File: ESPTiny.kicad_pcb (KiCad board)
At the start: 2 copper layers, 2 parts, among them J1 Conn_01x10_Male, U1 ESP-01v090

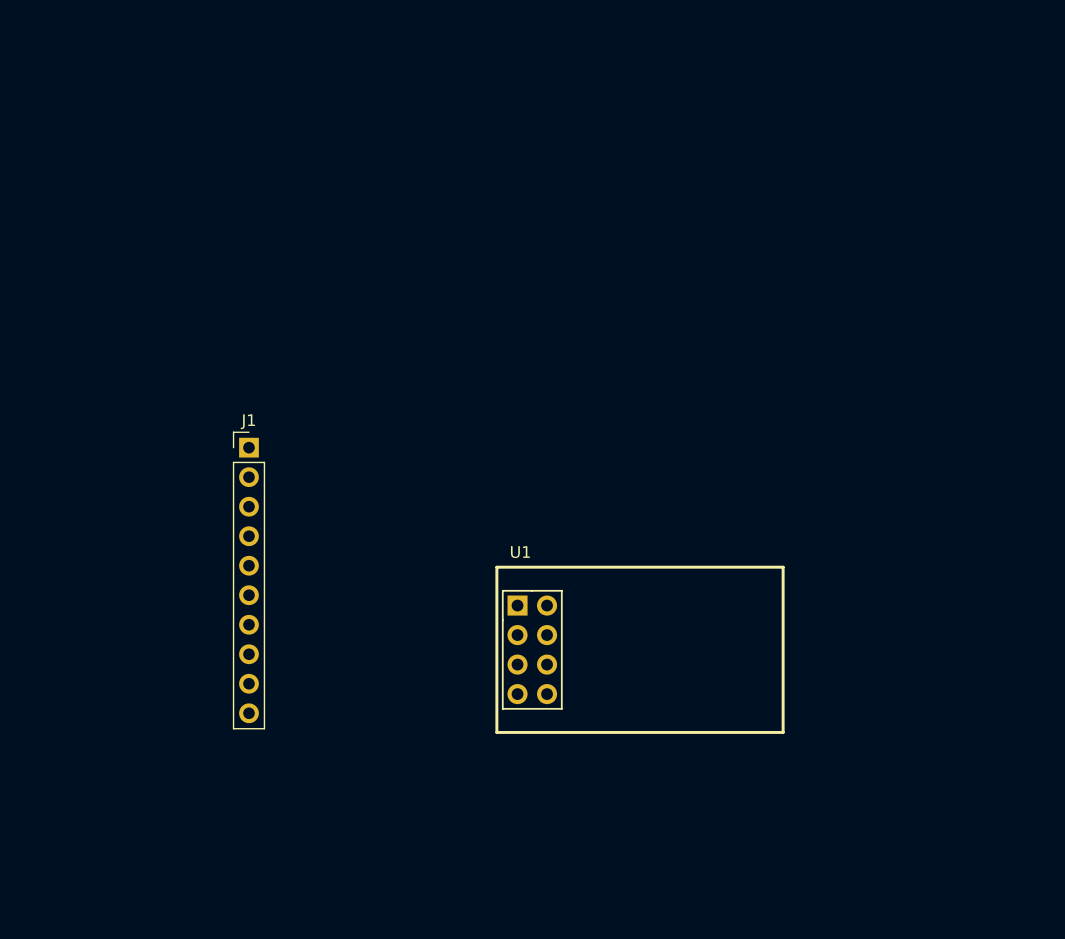
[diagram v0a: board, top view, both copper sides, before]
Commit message: Add footprints
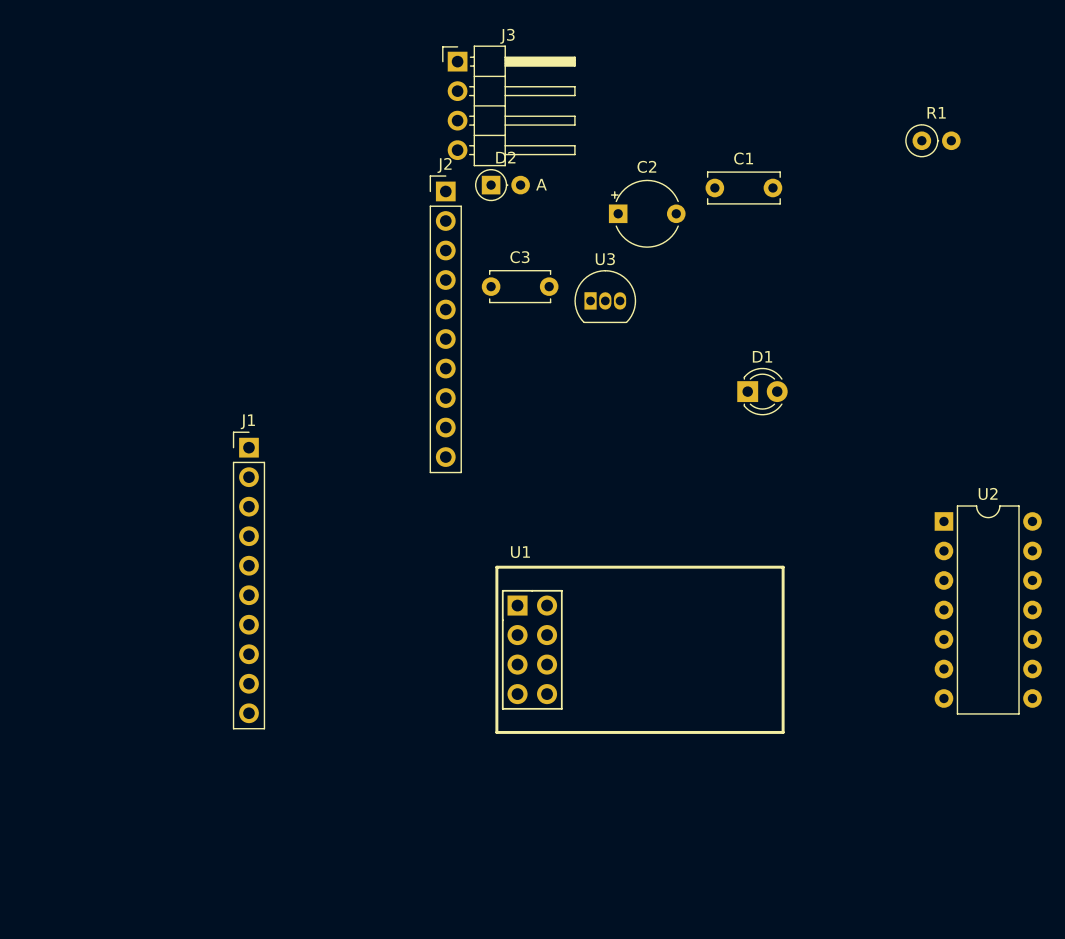
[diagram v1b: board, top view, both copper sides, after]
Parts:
- added C1: 1u, Capacitor_THT:C_Disc_D6.0mm_W2.5mm_P5.00mm, F.Cu at (92.8, 4.19)
- added C2: 100u, Capacitor_THT:CP_Radial_Tantal_D5.5mm_P5.00mm, F.Cu at (84.5, 6.41)
- added C3: 100n, Capacitor_THT:C_Disc_D5.0mm_W2.5mm_P5.00mm, F.Cu at (73.5, 12.7)
- added D1: LED, LED_THT:LED_D3.0mm, F.Cu at (95.6, 21.7)
- added D2: BAT85, Diode_THT:D_DO-35_SOD27_P2.54mm_Vertical_AnodeUp, F.Cu at (73.5, 3.94)
- added J2: Conn_01x10_Male, Connector_PinHeader_2.54mm:PinHeader_1x10_P2.54mm_Vertical, F.Cu at (69.6, 4.49)
- added J3: Conn_01x04_Male, Connector_PinHeader_2.54mm:PinHeader_1x04_P2.54mm_Horizontal, F.Cu at (70.7, -6.68)
- added R1: 220, Resistor_THT:R_Axial_DIN0207_L6.3mm_D2.5mm_P2.54mm_Vertical, F.Cu at (110.6, 0.13)
- added U2: ATtiny84-20PU, Package_DIP:DIP-14_W7.62mm, F.Cu at (112.5, 32.9)
- added U3: MCP1700-3302E_TO92, Package_TO_SOT_THT:TO-92_Inline, F.Cu at (82.1, 13.9)

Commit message: Without power divider
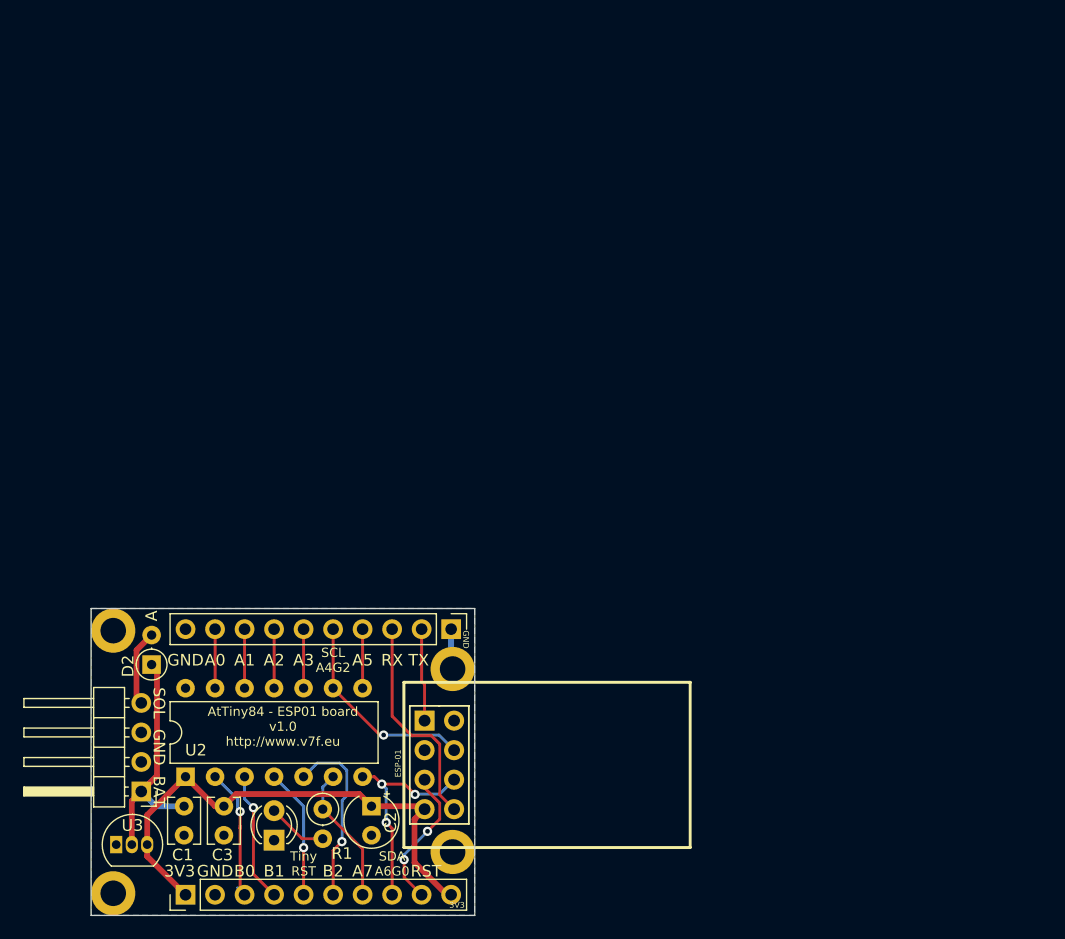
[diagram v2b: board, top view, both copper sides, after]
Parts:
- added REF**: MountingHole_2.2mm_M2_DIN965_Pad, MountingHole:MountingHole_2.2mm_M2_DIN965_Pad, F.Cu at (41.0, 42.3)
- added REF**: MountingHole_2.2mm_M2_DIN965_Pad, MountingHole:MountingHole_2.2mm_M2_DIN965_Pad, F.Cu at (41.0, 64.9)
- added REF**: MountingHole_2.2mm_M2_DIN965_Pad, MountingHole:MountingHole_2.2mm_M2_DIN965_Pad, F.Cu at (70.2, 61.3)
- added REF**: MountingHole_2.2mm_M2_DIN965_Pad, MountingHole:MountingHole_2.2mm_M2_DIN965_Pad, F.Cu at (70.2, 45.6)
- C1: footprint Capacitor_THT:C_Disc_D6.0mm_W2.5mm_P5.00mm -> Capacitor_THT:C_Disc_D3.8mm_W2.6mm_P2.50mm
- C2: footprint Capacitor_THT:CP_Radial_Tantal_D5.5mm_P5.00mm -> Capacitor_THT:CP_Radial_Tantal_D4.5mm_P2.50mm
- C3: footprint Capacitor_THT:C_Disc_D5.0mm_W2.5mm_P5.00mm -> Capacitor_THT:C_Disc_D3.8mm_W2.6mm_P2.50mm
- moved R1 77.3 mm to (59.1, 57.7), turned to 270 degrees
- moved C1 70.1 mm to (47.1, 57.4), turned to 270 degrees
- moved U2 68.9 mm to (47.2, 54.9), turned to 90 degrees
- moved J3 68.5 mm to (43.4, 56.1), turned to 180 degrees
- moved U3 62.0 mm to (41.4, 60.7)
- moved D1 56.1 mm to (54.9, 60.3), turned to 90 degrees
- moved C2 55.2 mm to (63.2, 57.4), turned to 270 degrees
- moved D2 50.6 mm to (44.3, 45.2), turned to 90 degrees
- moved C3 50.3 mm to (50.5, 57.4), turned to 270 degrees
- moved J1 38.9 mm to (47.2, 65.0), turned to 90 degrees
- moved J2 37.7 mm to (70.1, 42.2), turned to 270 degrees
- moved U1 12.7 mm to (67.8, 50.0)
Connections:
- C1 pad 1: Net-(C1-Pad1) -> +BATT
- C1 pad 2: Net-(C1-Pad2) -> GND
- C2 pad 1: Net-(C2-Pad1) -> +3V3
- C2 pad 2: Net-(C2-Pad2) -> GND
- C3 pad 1: Net-(C3-Pad1) -> +3V3
- C3 pad 2: Net-(C3-Pad2) -> GND
- D1 pad 1: Net-(D1-Pad1) -> GND
- D2 pad 1: Net-(D2-Pad1) -> +BATT
- J1 pad 1: Net-(J1-Pad1) -> +3V3
- J1 pad 10: Net-(J1-Pad10) -> +3V3
- J1 pad 2: Net-(J1-Pad2) -> GND
- J1 pad 3: Net-(J1-Pad3) -> /B0
- J1 pad 4: Net-(J1-Pad4) -> /B1
- J1 pad 5: Net-(J1-Pad5) -> /TRST
- J1 pad 6: Net-(J1-Pad6) -> /B2
- J1 pad 7: Net-(J1-Pad7) -> /A7
- J1 pad 8: Net-(J1-Pad8) -> /SDA-A6
- J1 pad 9: Net-(J1-Pad9) -> /RST
- J2 pad 1: Net-(J2-Pad1) -> GND
- J2 pad 10: Net-(J2-Pad10) -> GND
- J2 pad 2: Net-(J2-Pad2) -> /TX
- J2 pad 3: Net-(J2-Pad3) -> /RX
- J2 pad 4: Net-(J2-Pad4) -> /A5
- J2 pad 5: Net-(J2-Pad5) -> /SCL-A4
- J2 pad 6: Net-(J2-Pad6) -> /A3
- J2 pad 7: Net-(J2-Pad7) -> /A2
- J2 pad 8: Net-(J2-Pad8) -> /A1
- J2 pad 9: Net-(J2-Pad9) -> /A0
- J3 pad 1: Net-(J3-Pad1) -> +BATT
- J3 pad 2: Net-(J3-Pad2) -> GND
- J3 pad 3: Net-(J3-Pad3) -> GND
- J3 pad 4: Net-(J3-Pad4) -> Net-(D2-Pad2)
- R1 pad 1: Net-(R1-Pad1) -> /A7
- R1 pad 2: Net-(R1-Pad2) -> Net-(D1-Pad2)
- U1 pad 1: Net-(U1-Pad1) -> /TX
- U1 pad 3: Net-(U1-Pad3) -> GND
- U1 pad 4: Net-(U1-Pad4) -> /SCL-A4
- U1 pad 5: Net-(U1-Pad5) -> /RST
- U1 pad 6: Net-(U1-Pad6) -> /SDA-A6
- U1 pad 8: Net-(U1-Pad8) -> /RX
- U2 pad 1: Net-(U2-Pad1) -> +3V3
- U2 pad 10: Net-(U2-Pad10) -> /A3
- U2 pad 11: Net-(U2-Pad11) -> /A2
- U2 pad 12: Net-(U2-Pad12) -> /A1
- U2 pad 13: Net-(U2-Pad13) -> /A0
- U2 pad 14: Net-(U2-Pad14) -> GND
- U2 pad 2: Net-(U2-Pad2) -> /B0
- U2 pad 3: Net-(U2-Pad3) -> /B1
- U2 pad 4: Net-(U2-Pad4) -> /TRST
- U2 pad 5: Net-(U2-Pad5) -> /B2
- U2 pad 6: Net-(U2-Pad6) -> /A7
- U2 pad 7: Net-(U2-Pad7) -> /SDA-A6
- U2 pad 8: Net-(U2-Pad8) -> /A5
- U2 pad 9: Net-(U2-Pad9) -> /SCL-A4
- U3 pad 1: Net-(U3-Pad1) -> GND
- U3 pad 2: Net-(U3-Pad2) -> +BATT
- U3 pad 3: Net-(U3-Pad3) -> +3V3
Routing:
- net +3V3: track 0.00 -> 45.1 mm
- net +BATT: track 0.00 -> 21.2 mm
- net /SDA-A6: track 0.00 -> 18.9 mm, vias 0 -> 3
- net /RX: track 0.00 -> 18.7 mm
- net /SCL-A4: track 0.00 -> 18.0 mm, vias 0 -> 1
- net /B2: track 0.00 -> 15.7 mm, vias 0 -> 1
- net /RST: track 0.00 -> 12.4 mm, vias 0 -> 2
- net /B0: track 0.00 -> 12.3 mm, vias 0 -> 1
- net /A7: track 0.00 -> 11.9 mm
- net /TRST: track 0.00 -> 11.9 mm, vias 0 -> 1
- net /B1: track 0.00 -> 11.8 mm, vias 0 -> 1
- net /TX: track 0.00 -> 7.98 mm
- net Net-(D2-Pad2): track 0.00 -> 6.69 mm
- net Net-(D1-Pad2): track 0.00 -> 5.19 mm
- net /A5: track 0.00 -> 5.08 mm
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- added copper zone on B.Cu, net GND
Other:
- board outline added: 33 x 26.4 mm
- net class Default: clearance 0.2 -> 0.25
- net class power added: clearance 0.25, trace_width 0.5, via_dia 0.8, via_drill 0.4
- rule trace_clearance: 0.2 -> 0.25
- rule trace_min: 0.2 -> 0.25
- board text added: "3V3"
- board text added: "A0"
- board text added: "A1"
- board text added: "A2"
- board text added: "A3"
- board text added: "A5"
- board text added: "A7"
- board text added: "AtTiny84 - ESP01 board v1.0 http://www.v7f.eu"
- board text added: "B0"
- board text added: "B1"
- board text added: "B2"
- board text added: "BAT"
- board text added: "ESP-01"
- board text added: "GND"
- board text added: "RST"
- board text added: "RX"
- board text added: "SCL A4G2"
- board text added: "SDA A6G0"
- board text added: "SOL"
- board text added: "TX"
- board text added: "Tiny RST"

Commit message: With power divider
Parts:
- added R2: 220, Resistor_THT:R_Axial_DIN0207_L6.3mm_D2.5mm_P2.54mm_Vertical, F.Cu at (49.9, 44.8)
- added R3: 220, Resistor_THT:R_Axial_DIN0207_L6.3mm_D2.5mm_P2.54mm_Vertical, F.Cu at (55.1, 44.8)
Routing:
- net +BATT: track 21.2 -> 24.4 mm
- net /A1: track 5.08 -> 7.96 mm
- net /A2: track 5.08 -> 6.26 mm
- net /A0: track 5.08 -> 5.95 mm
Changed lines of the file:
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@@
     (thickness 1.6)
     (drawings 49)
-    (tracks 122)
+    (tracks 133)
     (zones 0)
-    (modules 16)
+    (modules 18)
     (nets 21)
   )
@@
   )
   (layers
-    (0 F.Cu signal hide)
-    (31 B.Cu signal hide)
+    (0 F.Cu signal)
+    (31 B.Cu signal)
     (32 B.Adhes user)
     (33 F.Adhes user)
@@
       (effects (font (size 1 1) (thickness 0.15)))
     )
-    (fp_text user A (at 4.191 0 90) (layer F.SilkS)
+    (fp_text user A (at 4.064 0 90) (layer F.SilkS)
       (effects (font (size 1 1) (thickness 0.15)))
     )
@@
     )
   )
+  (module Resistor_THT:R_Axial_DIN0207_L6.3mm_D2.5mm_P2.54mm_Vertical (layer F.Cu)
+    (at 49.911 44.831 180)
+    (descr "Resistor, Axial_DIN0207 series, Axial, Vertical, pin pitch=2.54mm, 0.25W = 1/4W, length*diameter=6.3*2.5mm^2, http://cdn-reichelt.de/documents/datenblatt/B400/1_4W%23YAG.pdf")
+    (tags "Resistor Axial_DIN0207 series Axial Vertical pin pitch 2.54mm 0.25W = 1/4W length 6.3mm diameter 2.5mm")
+    (fp_text reference R2 (at 1.397 -1.27) (layer F.SilkS)
+      (effects (font (size 0.5 0.5) (thickness 0.125)))
+    )
+    (fp_text value 220 (at 1.27 2.37) (layer F.Fab)
+      (effects (font (size 1 1) (thickness 0.15)))
+    )
+    (fp_line (start 3.59 -1.5) (end -1.5 -1.5) (layer F.CrtYd) (width 0.05))
+    (fp_line (start 3.59 1.5) (end 3.59 -1.5) (layer F.CrtYd) (width 0.05))
+    (fp_line (start -1.5 1.5) (end 3.59 1.5) (layer F.CrtYd) (width 0.05))
+    (fp_line (start -1.5 -1.5) (end -1.5 1.5) (layer F.CrtYd) (width 0.05))
+    (fp_line (start 1.37 0) (end 1.44 0) (layer F.SilkS) (width 0.12))
+    (fp_line (start 0 0) (end 2.54 0) (layer F.Fab) (width 0.1))
+    (fp_circle (center 0 0) (end 1.37 0) (layer F.SilkS) (width 0.12))
+    (fp_circle (center 0 0) (end 1.25 0) (layer F.Fab) (width 0.1))
+    (fp_text user %R (at 1.27 -2.37) (layer F.Fab)
+      (effects (font (size 1 1) (thickness 0.15)))
+    )
+    (pad 1 thru_hole circle (at 0 0 180) (size 1.6 1.6) (drill 0.8) (layers *.Cu *.Mask)
+      (net 19 /A1))
+    (pad 2 thru_hole oval (at 2.54 0 180) (size 1.6 1.6) (drill 0.8) (layers *.Cu *.Mask)
+      (net 5 +BATT))
+    (model ${KISYS3DMOD}/Resistor_THT.3dshapes/R_Axial_DIN0207_L6.3mm_D2.5mm_P2.54mm_Vertical.wrl
+      (at (xyz 0 0 0))
+      (scale (xyz 1 1 1))
+      (rotate (xyz 0 0 0))
+    )
+  )
+  (module Resistor_THT:R_Axial_DIN0207_L6.3mm_D2.5mm_P2.54mm_Vertical (layer F.Cu)
+    (at 55.118 44.831 180)
+    (descr "Resistor, Axial_DIN0207 series, Axial, Vertical, pin pitch=2.54mm, 0.25W = 1/4W, length*diameter=6.3*2.5mm^2, http://cdn-reichelt.de/documents/datenblatt/B400/1_4W%23YAG.pdf")
+    (tags "Resistor Axial_DIN0207 series Axial Vertical pin pitch 2.54mm 0.25W = 1/4W length 6.3mm diameter 2.5mm")
+    (fp_text reference R3 (at 1.651 -1.27) (layer F.SilkS)
+      (effects (font (size 0.5 0.5) (thickness 0.125)))
+    )
+    (fp_text value 220 (at 1.27 2.37) (layer F.Fab)
+      (effects (font (size 1 1) (thickness 0.15)))
+    )
+    (fp_text user %R (at 1.27 -2.37) (layer F.Fab)
+      (effects (font (size 1 1) (thickness 0.15)))
+    )
+    (fp_circle (center 0 0) (end 1.25 0) (layer F.Fab) (width 0.1))
+    (fp_circle (center 0 0) (end 1.37 0) (layer F.SilkS) (width 0.12))
+    (fp_line (start 0 0) (end 2.54 0) (layer F.Fab) (width 0.1))
+    (fp_line (start 1.37 0) (end 1.44 0) (layer F.SilkS) (width 0.12))
+    (fp_line (start -1.5 -1.5) (end -1.5 1.5) (layer F.CrtYd) (width 0.05))
+    (fp_line (start -1.5 1.5) (end 3.59 1.5) (layer F.CrtYd) (width 0.05))
+    (fp_line (start 3.59 1.5) (end 3.59 -1.5) (layer F.CrtYd) (width 0.05))
+    (fp_line (start 3.59 -1.5) (end -1.5 -1.5) (layer F.CrtYd) (width 0.05))
+    (pad 2 thru_hole oval (at 2.54 0 180) (size 1.6 1.6) (drill 0.8) (layers *.Cu *.Mask)
+      (net 19 /A1))
+    (pad 1 thru_hole circle (at 0 0 180) (size 1.6 1.6) (drill 0.8) (layers *.Cu *.Mask)
+      (net 1 GND))
+    (model ${KISYS3DMOD}/Resistor_THT.3dshapes/R_Axial_DIN0207_L6.3mm_D2.5mm_P2.54mm_Vertical.wrl
+      (at (xyz 0 0 0))
+      (scale (xyz 1 1 1))
+      (rotate (xyz 0 0 0))
+    )
+  )
   (gr_text GND (at 71.374 43.053 270) (layer B.SilkS)
     (effects (font (size 0.5 0.5) (thickness 0.125)) (justify mirror))
@@
     (effects (font (size 1 1) (thickness 0.15)) (justify mirror))
   )
-  (gr_text A2 (at 54.864 44.831) (layer B.SilkS)
-    (effects (font (size 1 1) (thickness 0.15)) (justify mirror))
-  )
-  (gr_text A1 (at 52.197 44.831) (layer B.SilkS)
-    (effects (font (size 1 1) (thickness 0.15)) (justify mirror))
-  )
-  (gr_text A0 (at 49.784 44.831) (layer B.SilkS)
-    (effects (font (size 1 1) (thickness 0.15)) (justify mirror))
-  )
-  (gr_text GND (at 47.244 44.831) (layer B.SilkS)
-    (effects (font (size 1 1) (thickness 0.15)) (justify mirror))
+  (gr_text A2 (at 54.864 43.434) (layer B.SilkS)
+    (effects (font (size 0.5 0.5) (thickness 0.125)) (justify mirror))
+  )
+  (gr_text A1 (at 52.197 43.434) (layer B.SilkS)
+    (effects (font (size 0.5 0.5) (thickness 0.125)) (justify mirror))
+  )
+  (gr_text A0 (at 49.784 43.434) (layer B.SilkS)
+    (effects (font (size 0.5 0.5) (thickness 0.125)) (justify mirror))
+  )
+  (gr_text GND (at 47.244 43.434) (layer B.SilkS)
+    (effects (font (size 0.5 0.5) (thickness 0.125)) (justify mirror))
   )
   (gr_text 3V3 (at 70.612 65.913) (layer F.SilkS)
@@
     (effects (font (size 0.8 0.8) (thickness 0.15)))
   )
-  (gr_text A3 (at 57.404 44.831) (layer F.SilkS)
-    (effects (font (size 1 1) (thickness 0.15)))
-  )
-  (gr_text A2 (at 54.864 44.831) (layer F.SilkS)
-    (effects (font (size 1 1) (thickness 0.15)))
-  )
-  (gr_text A1 (at 52.324 44.831) (layer F.SilkS)
-    (effects (font (size 1 1) (thickness 0.15)))
-  )
-  (gr_text A0 (at 49.784 44.831) (layer F.SilkS)
-    (effects (font (size 1 1) (thickness 0.15)))
-  )
-  (gr_text GND (at 47.244 44.831) (layer F.SilkS)
-    (effects (font (size 1 1) (thickness 0.15)))
+  (gr_text A3 (at 57.531 44.831) (layer F.SilkS)
+    (effects (font (size 1 1) (thickness 0.15)))
+  )
+  (gr_text A2 (at 53.467 43.815) (layer F.SilkS)
+    (effects (font (size 0.5 0.5) (thickness 0.125)))
+  )
+  (gr_text A1 (at 52.451 43.815) (layer F.SilkS)
+    (effects (font (size 0.5 0.5) (thickness 0.125)))
+  )
+  (gr_text A0 (at 51.435 43.815) (layer F.SilkS)
+    (effects (font (size 0.5 0.5) (thickness 0.125)))
+  )
+  (gr_text GND (at 47.244 43.815) (layer F.SilkS)
+    (effects (font (size 0.5 0.5) (thickness 0.125)))
   )
   (gr_line (start 72.136 40.386) (end 72.136 66.802) (layer Edge.Cuts) (width 0.05))
@@
   (segment (start 44.784001 54.783999) (end 44.784001 45.673001) (width 0.5) (layer F.Cu) (net 5))
   (segment (start 43.434 56.134) (end 44.784001 54.783999) (width 0.5) (layer F.Cu) (net 5))
+  (segment (start 44.704 44.831) (end 44.323 45.212) (width 0.5) (layer F.Cu) (net 5))
+  (segment (start 47.371 44.831) (end 44.704 44.831) (width 0.5) (layer F.Cu) (net 5))
   (segment (start 51.721001 64.421001) (end 52.324 65.024) (width 0.25) (layer B.Cu) (net 6))
   (segment (start 51.943998 64.643998) (end 52.324 65.024) (width 0.25) (layer F.Cu) (net 6))
@@
   (segment (start 69.056601 51.276601) (end 64.293399 51.276601) (width 0.25) (layer B.Cu) (net 16))
   (segment (start 57.404 42.164) (end 57.404 47.244) (width 0.25) (layer F.Cu) (net 17))
-  (segment (start 54.864 42.164) (end 54.864 47.244) (width 0.25) (layer F.Cu) (net 18))
-  (segment (start 52.324 42.164) (end 52.324 47.244) (width 0.25) (layer F.Cu) (net 19))
-  (segment (start 49.784 47.244) (end 49.784 42.164) (width 0.25) (layer F.Cu) (net 20))
+  (segment (start 56.293001 43.593001) (end 54.864 42.164) (width 0.25) (layer F.Cu) (net 18))
+  (segment (start 56.293001 45.395001) (end 56.293001 43.593001) (width 0.25) (layer F.Cu) (net 18))
+  (segment (start 54.864 46.824002) (end 56.293001 45.395001) (width 0.25) (layer F.Cu) (net 18))
+  (segment (start 54.864 47.244) (end 54.864 46.824002) (width 0.25) (layer F.Cu) (net 18))
+  (segment (start 52.324 44.577) (end 52.578 44.831) (width 0.25) (layer F.Cu) (net 19))
+  (segment (start 52.324 42.164) (end 52.324 44.577) (width 0.25) (layer F.Cu) (net 19))
+  (segment (start 52.324 45.085) (end 52.578 44.831) (width 0.25) (layer F.Cu) (net 19))
+  (segment (start 52.324 47.244) (end 52.324 45.085) (width 0.25) (layer F.Cu) (net 19))
+  (segment (start 52.578 44.831) (end 49.911 44.831) (width 0.25) (layer F.Cu) (net 19))
+  (segment (start 48.735999 43.212001) (end 49.784 42.164) (width 0.25) (layer F.Cu) (net 20))
+  (segment (start 48.735999 46.195999) (end 48.735999 43.212001) (width 0.25) (layer F.Cu) (net 20))
+  (segment (start 49.784 47.244) (end 48.735999 46.195999) (width 0.25) (layer F.Cu) (net 20))
   (zone (net 1) (net_name GND) (layer B.Cu) (hatch edge 0.508)
     (connect_pads (clearance 0.508))
